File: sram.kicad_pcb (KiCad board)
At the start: 4 copper layers, 92 x 47 mm, 28 parts, among them J1 Cache_slot, U1 IS61C256AL-12JLI, U10 74F244, U11 74F244, U2 IS61C256AL-12JLI, U3 IS61C256AL-12JLI, U4 IS61C256AL-12JLI, U5 IS61C256AL-12JLI, U6 IS61C256AL-12JLI, U7 IS61C256AL-12JLI, U8 IS61C256AL-12JLI, U9 IS61C3216AL-12TLI

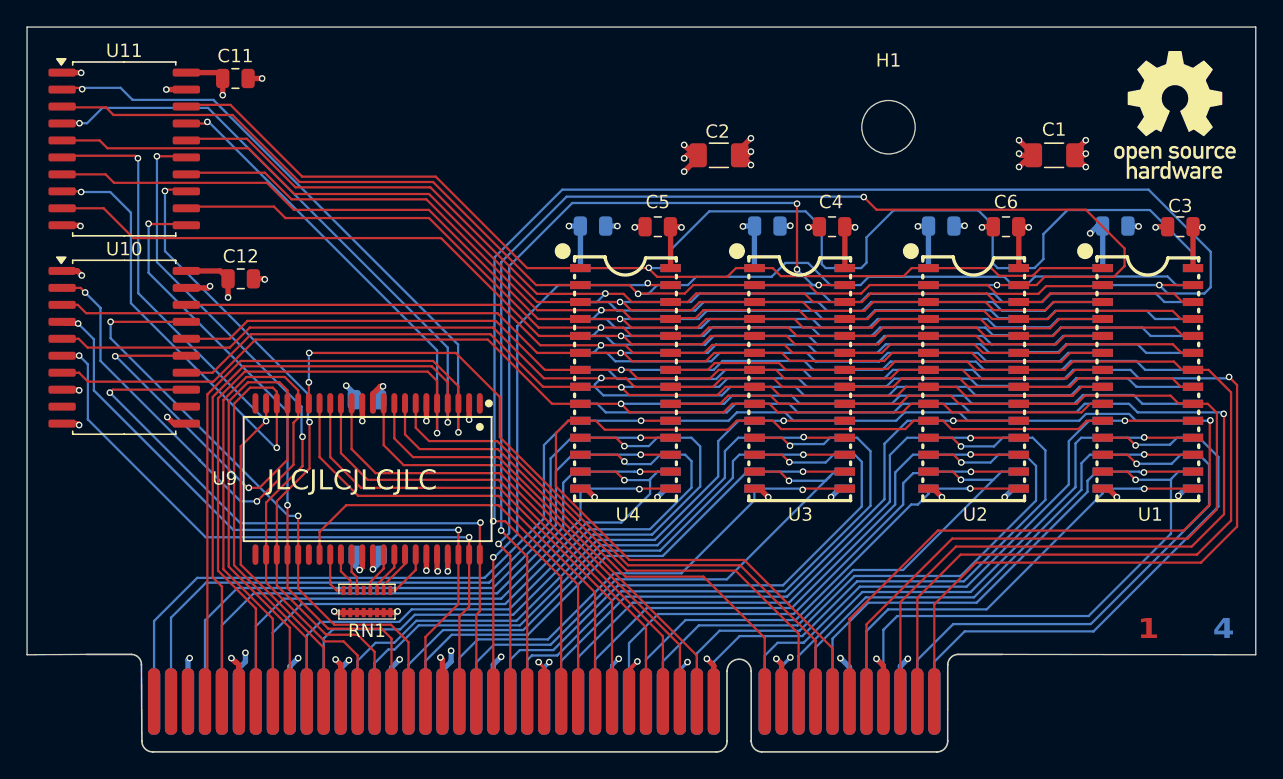
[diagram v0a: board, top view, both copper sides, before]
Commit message: change from rasz_pl:  - moving VIAs apart  - change resistor network with single resistor
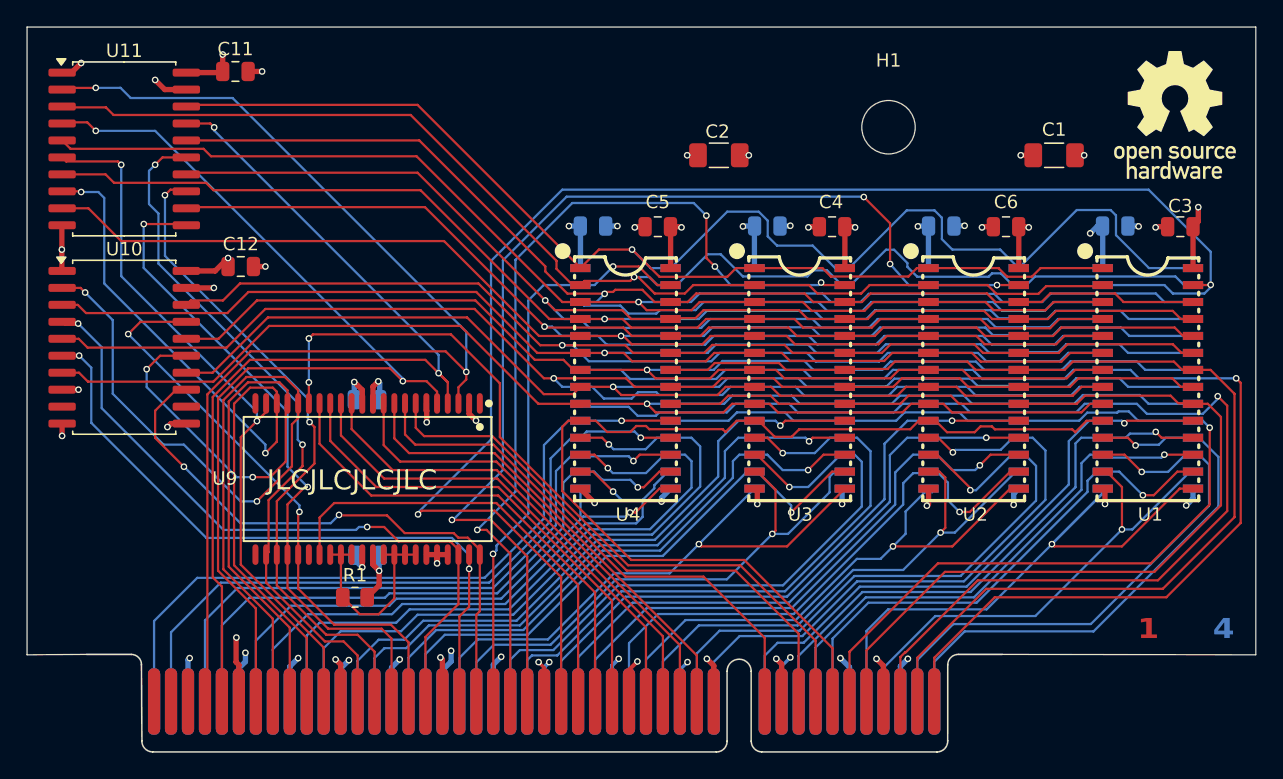
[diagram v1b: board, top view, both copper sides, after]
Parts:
- removed RN1: EXB2HV103JV, footprints:RES-ARRAY-SMD_16P-L3.8-W1.6-P0.50-BL
- added R1: 10k, Resistor_SMD:R_0805_2012Metric, F.Cu at (163.6, 99.7)
- moved C12 0.92 mm to (155.0, 74.9)
- moved C11 0.52 mm to (154.6, 60.3)
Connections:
- U11 pad 17: CPU_A15 -> CPU_A16
- U11 pad 4: CPU_A16 -> CPU_A15
- U9 pad 30: TIO9 -> TIO10
- U9 pad 32: TIO11 -> TIO10
- U9 pad 35: TIO12 -> TIO10
- U9 pad 36: TIO13 -> TIO10
- U9 pad 37: TIO14 -> TIO10
- U9 pad 38: TIO15 -> TIO10
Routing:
- net CWE1: track 100.6 -> 83.9 mm, vias 3 -> 4
- net CPU_A16: track 87.6 -> 72.7 mm
- net TIO10: track 2.97 -> 15.4 mm
- net CPU_D3: track 34.4 -> 45.4 mm
- net GND: track 99.6 -> 92.2 mm, vias 54 -> 44
- net CWE0: track 107.3 -> 114.0 mm
- net CPU_A4: track 51.2 -> 44.8 mm
- net CPU_D11: track 36.6 -> 42.8 mm
- net CPU_D19: track 38.0 -> 43.4 mm
- net +5V: track 81.3 -> 76.6 mm, vias 27 -> 23
- net CPU_A13: track 58.0 -> 53.4 mm
- net CPU_D2: track 41.2 -> 36.9 mm
- net Cache_A15: track 129.3 -> 133.4 mm
- net CWE2: track 70.6 -> 66.7 mm
- net TIO15: track 3.68 -> 0.00 mm
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
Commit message: pass DRC with rounded tracks
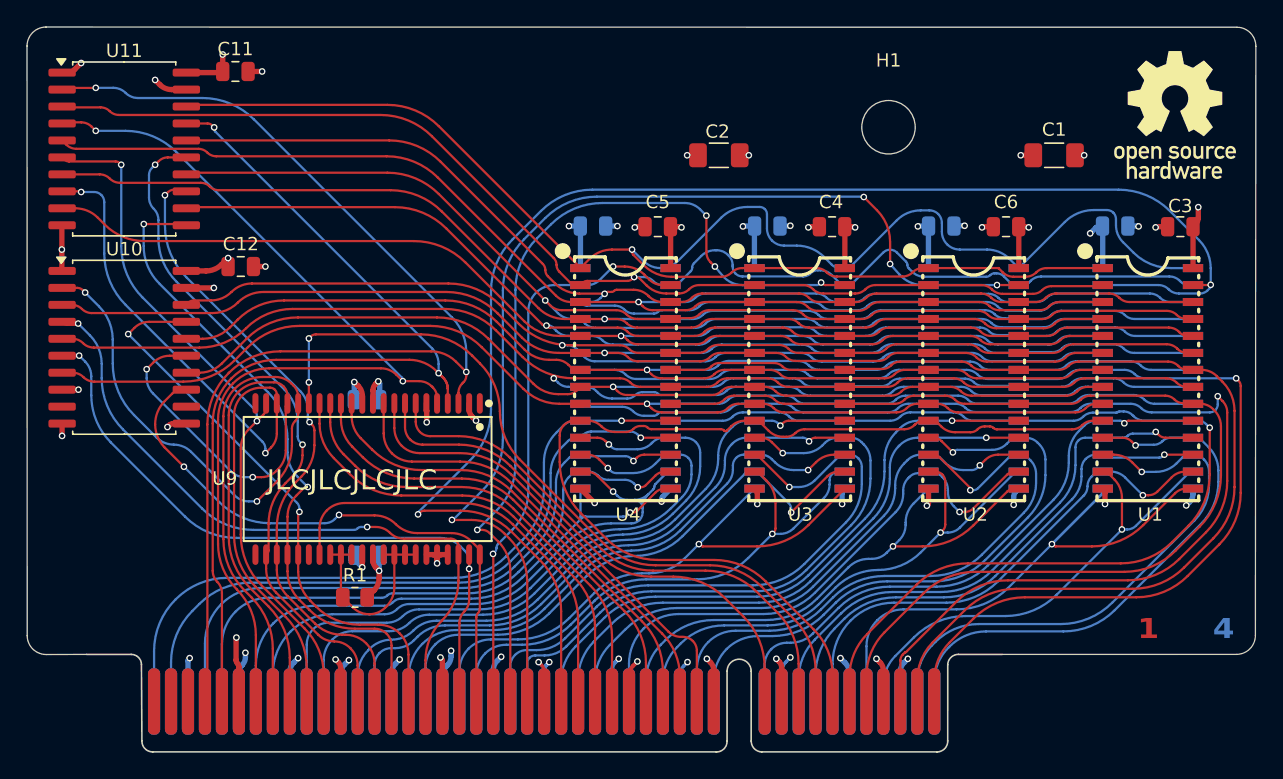
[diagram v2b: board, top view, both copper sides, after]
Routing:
- net Cache_A13: track 133.5 -> 130.8 mm
- net Cache_A4: track 126.4 -> 124.1 mm
- net Cache_A16: track 125.4 -> 123.3 mm
- net Cache_A14: track 122.0 -> 120.0 mm
- net CWE0: track 114.0 -> 111.9 mm
- net Cache_A5: track 119.5 -> 117.5 mm
- net Cache_A7: track 127.9 -> 125.9 mm
- net Cache_A6: track 116.0 -> 113.9 mm
- net CA3A: track 77.8 -> 75.8 mm
- net Cache_A8: track 127.8 -> 125.9 mm
- net CPU_A14: track 64.9 -> 63.0 mm
- net Cache_A12: track 124.7 -> 122.8 mm
- net Cache_A17: track 132.3 -> 130.4 mm
- net COEA: track 85.0 -> 83.3 mm
- net COEB: track 92.4 -> 90.6 mm
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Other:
- outline, holes or cut-outs redrawn

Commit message: updated to 256KB/1MB
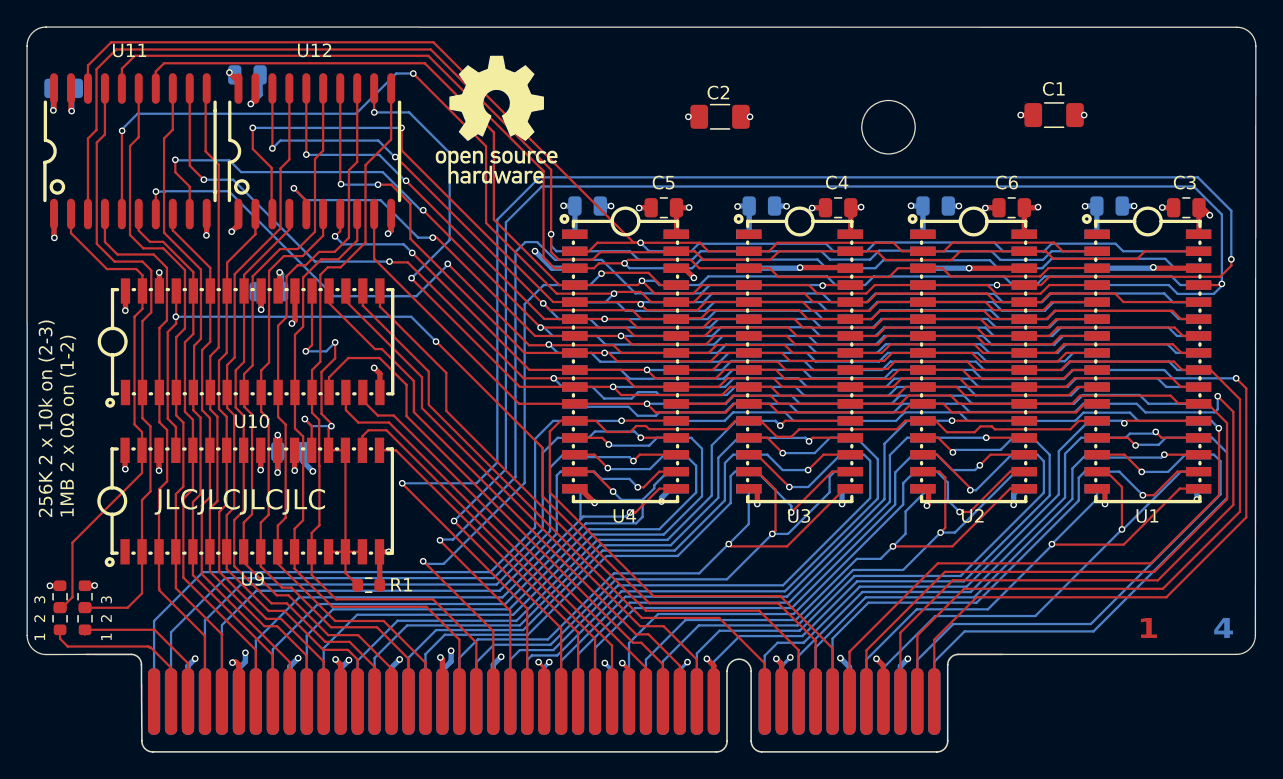
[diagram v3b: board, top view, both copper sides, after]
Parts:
- added R2: 0, Resistor_SMD:R_0603_1608Metric, F.Cu at (143.3, 101.3)
- added R3: 0, Resistor_SMD:R_0603_1608Metric, F.Cu at (141.5, 101.3)
- added R4: 10k, Resistor_SMD:R_0603_1608Metric, F.Cu at (143.3, 99.7)
- added R5: 10k, Resistor_SMD:R_0603_1608Metric, F.Cu at (141.5, 99.7)
- added U12: SN74AHCT244DWR, others:SOIC-20_L12.8-W7.5-P1.27-LS10.3-BL, F.Cu at (160.5, 66.3)
- C11, C12: moved to B.Cu
- J1: footprint footprints:Cache slot -> others:Cache slot
- R1: footprint Resistor_SMD:R_0805_2012Metric -> Resistor_SMD:R_0603_1608Metric
- U1, U2, U3, U4, U5, U6, U7, U8: value IS61C256AL-12JLI -> IS61C1024AL-12JLI; footprint footprints:SOJ-28_L18.1-W7.6-P1.27-LS8.6-BL -> others:SOJ-32_L21.0-W7.6-P1.27-LS8.5-BL
- U10: value 74F244 -> IS61C1024AL-12JLI; footprint Package_SO:SOIC-20W_7.5x12.8mm_P1.27mm -> others:SOJ-32_L21.0-W7.6-P1.27-LS8.5-BL
- U11: value 74F244 -> SN74AHCT244DWR; footprint Package_SO:SOIC-20W_7.5x12.8mm_P1.27mm -> others:SOIC-20_L12.8-W7.5-P1.27-LS10.3-BL
- U9: value IS61C3216AL-12TLI -> IS61C1024AL-12JLI; footprint footprints:TSOP-44_L18.4-W10.2-P0.80-LS11.8-BL -> others:SOJ-32_L21.0-W7.6-P1.27-LS8.5-BL
- moved C12 18.8 mm to (141.7, 61.6)
- moved C13 10.9 mm to (157.1, 76.8)
- moved C14 9.68 mm to (158.7, 88.8)
- moved U10 9.62 mm to (155.9, 80.6)
- moved U9 8.80 mm to (155.9, 92.5), turned to 0 degrees
- moved C1 3.01 mm to (215.9, 63.6)
- moved C2 2.88 mm to (190.9, 63.7)
- moved C7 1.56 mm to (220.1, 70.4)
- moved C8 1.56 mm to (207.0, 70.4)
- moved C10 1.55 mm to (194.0, 70.4)
- moved C9 1.55 mm to (181.0, 70.4)
- moved C5 1.49 mm to (186.7, 70.5)
- moved C4 1.49 mm to (199.7, 70.5)
- moved C3 1.49 mm to (225.8, 70.5)
- moved C6 1.48 mm to (212.7, 70.5)
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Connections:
- J1 pad a45: unconnected-(J1-Pada45) -> CPU_A18
- J1 pad a46: unconnected-(J1-Pada46) -> CPU_A19
- U1 pad 1: Cache_A17 -> unconnected-(U1-NC-Pad1)
- U1 pad 10: CA3A -> Cache_A5
- U1 pad 11: CPU_D0 -> Cache_A4
- U1 pad 12: CPU_D1 -> CA3A
- U1 pad 13: CPU_D2 -> CPU_D0
- U1 pad 14: GND -> CPU_D1
- U1 pad 15: CPU_D3 -> CPU_D2
- U1 pad 16: CPU_D4 -> GND
- U1 pad 17: CPU_D5 -> CPU_D3
- U1 pad 18: CPU_D6 -> CPU_D4
- U1 pad 19: CPU_D7 -> CPU_D5
- U1 pad 2: Cache_A15 -> Cache_A19
- U1 pad 20: CCSA -> CPU_D6
- U1 pad 21: Cache_A13 -> CPU_D7
- U1 pad 22: COEA -> CCSA
- U1 pad 23: Cache_A14 -> Cache_A13
- U1 pad 24: Cache_A12 -> COEA
- U1 pad 25: Cache_A11 -> Cache_A14
- U1 pad 26: Cache_A16 -> Cache_A12
- U1 pad 27: CWE0 -> Cache_A11
- U1 pad 28: +5V -> Cache_A16
- U1 pad 3: Cache_A10 -> Cache_A17
- U1 pad 4: Cache_A9 -> Cache_A15
- U1 pad 5: Cache_A8 -> Cache_A10
- U1 pad 6: Cache_A7 -> Cache_A9
- U1 pad 7: Cache_A6 -> Cache_A8
- U1 pad 8: Cache_A5 -> Cache_A7
- U1 pad 9: Cache_A4 -> Cache_A6
- U10 pad 1: GND -> unconnected-(U10-NC-Pad1)
- U10 pad 10: GND -> CPU_A6
- U10 pad 11: GND -> CPU_A5
- U10 pad 12: unconnected-(U10-1Y3-Pad12) -> CPU_A4
- U10 pad 13: CPU_A4 -> TAG_Q4
- U10 pad 14: Cache_A5 -> TAG_Q6
- U10 pad 15: CPU_A13 -> TAG_Q5
- U10 pad 16: Cache_A6 -> GND
- U10 pad 17: CPU_A7 -> TAG_Q0
- U10 pad 18: Cache_A14 -> TAG_Q1
- U10 pad 19: GND -> TAG_Q2
- U10 pad 2: CPU_A14 -> JPU_A18
- U10 pad 20: +5V -> TAG_Q3
- U10 pad 3: Cache_A7 -> CPU_A17
- U10 pad 4: CPU_A6 -> CPU_A16
- U10 pad 5: Cache_A13 -> CPU_A14
- U10 pad 6: CPU_A5 -> CPU_A12
- U10 pad 7: Cache_A4 -> CPU_A10
- U10 pad 8: GND -> CPU_A8
- U10 pad 9: unconnected-(U10-2Y3-Pad9) -> CPU_A7
- U11 pad 11: CPU_A8 -> CPU_A12
- U11 pad 12: Cache_A12 -> Cache_A13
- U11 pad 13: CPU_A9 -> CPU_A14
- U11 pad 14: Cache_A11 -> Cache_A15
- U11 pad 15: CPU_A10 -> CPU_A16
- U11 pad 16: Cache_A16 -> Cache_A17
- U11 pad 17: CPU_A16 -> JPU_A18
- U11 pad 18: Cache_A17 -> Cache_A19
- U11 pad 2: CPU_A17 -> JPU_A19
- U11 pad 3: Cache_A15 -> Cache_A18
- U11 pad 4: CPU_A15 -> CPU_A17
- U11 pad 5: Cache_A10 -> Cache_A16
- U11 pad 6: CPU_A11 -> CPU_A15
- U11 pad 7: Cache_A9 -> Cache_A14
- U11 pad 8: CPU_A12 -> CPU_A13
- U11 pad 9: Cache_A8 -> Cache_A12
- U2 pad 1: Cache_A17 -> unconnected-(U2-NC-Pad1)
- U2 pad 10: CA3A -> Cache_A5
- U2 pad 11: CPU_D8 -> Cache_A4
- U2 pad 12: CPU_D9 -> CA3A
- U2 pad 13: CPU_D10 -> CPU_D8
- U2 pad 14: GND -> CPU_D9
- U2 pad 15: CPU_D11 -> CPU_D10
- U2 pad 16: CPU_D12 -> GND
- U2 pad 17: CPU_D13 -> CPU_D11
- U2 pad 18: CPU_D14 -> CPU_D12
- U2 pad 19: CPU_D15 -> CPU_D13
- U2 pad 2: Cache_A15 -> Cache_A19
- U2 pad 20: CCSA -> CPU_D14
- U2 pad 21: Cache_A13 -> CPU_D15
- U2 pad 22: COEA -> CCSA
- U2 pad 23: Cache_A14 -> Cache_A13
- U2 pad 24: Cache_A12 -> COEA
- U2 pad 25: Cache_A11 -> Cache_A14
- U2 pad 26: Cache_A16 -> Cache_A12
- U2 pad 27: CWE1 -> Cache_A11
- U2 pad 28: +5V -> Cache_A16
- U2 pad 3: Cache_A10 -> Cache_A17
- U2 pad 4: Cache_A9 -> Cache_A15
- U2 pad 5: Cache_A8 -> Cache_A10
- U2 pad 6: Cache_A7 -> Cache_A9
- U2 pad 7: Cache_A6 -> Cache_A8
- U2 pad 8: Cache_A5 -> Cache_A7
- U2 pad 9: Cache_A4 -> Cache_A6
- U3 pad 1: Cache_A17 -> unconnected-(U3-NC-Pad1)
- U3 pad 10: CA3A -> Cache_A5
- U3 pad 11: CPU_D16 -> Cache_A4
- U3 pad 12: CPU_D17 -> CA3A
- U3 pad 13: CPU_D18 -> CPU_D16
- U3 pad 14: GND -> CPU_D17
- U3 pad 15: CPU_D19 -> CPU_D18
- U3 pad 16: CPU_D20 -> GND
- U3 pad 17: CPU_D21 -> CPU_D19
- U3 pad 18: CPU_D22 -> CPU_D20
- U3 pad 19: CPU_D23 -> CPU_D21
- U3 pad 2: Cache_A15 -> Cache_A19
- U3 pad 20: CCSA -> CPU_D22
- U3 pad 21: Cache_A13 -> CPU_D23
- U3 pad 22: COEA -> CCSA
- U3 pad 23: Cache_A14 -> Cache_A13
- U3 pad 24: Cache_A12 -> COEA
- U3 pad 25: Cache_A11 -> Cache_A14
- U3 pad 26: Cache_A16 -> Cache_A12
- U3 pad 27: CWE2 -> Cache_A11
- U3 pad 28: +5V -> Cache_A16
- U3 pad 3: Cache_A10 -> Cache_A17
- U3 pad 4: Cache_A9 -> Cache_A15
- U3 pad 5: Cache_A8 -> Cache_A10
- U3 pad 6: Cache_A7 -> Cache_A9
- U3 pad 7: Cache_A6 -> Cache_A8
- U3 pad 8: Cache_A5 -> Cache_A7
- U3 pad 9: Cache_A4 -> Cache_A6
- U4 pad 1: Cache_A17 -> unconnected-(U4-NC-Pad1)
- U4 pad 10: CA3A -> Cache_A5
- U4 pad 11: CPU_D24 -> Cache_A4
- U4 pad 12: CPU_D25 -> CA3A
- U4 pad 13: CPU_D26 -> CPU_D24
- U4 pad 14: GND -> CPU_D25
- U4 pad 15: CPU_D27 -> CPU_D26
- U4 pad 16: CPU_D28 -> GND
- U4 pad 17: CPU_D29 -> CPU_D27
- U4 pad 18: CPU_D30 -> CPU_D28
- U4 pad 19: CPU_D31 -> CPU_D29
- U4 pad 2: Cache_A15 -> Cache_A19
- U4 pad 20: CCSA -> CPU_D30
- U4 pad 21: Cache_A13 -> CPU_D31
- U4 pad 22: COEA -> CCSA
- U4 pad 23: Cache_A14 -> Cache_A13
- U4 pad 24: Cache_A12 -> COEA
- U4 pad 25: Cache_A11 -> Cache_A14
- U4 pad 26: Cache_A16 -> Cache_A12
- U4 pad 27: CWE3 -> Cache_A11
- U4 pad 28: +5V -> Cache_A16
- U4 pad 3: Cache_A10 -> Cache_A17
- U4 pad 4: Cache_A9 -> Cache_A15
- U4 pad 5: Cache_A8 -> Cache_A10
- U4 pad 6: Cache_A7 -> Cache_A9
- U4 pad 7: Cache_A6 -> Cache_A8
- U4 pad 8: Cache_A5 -> Cache_A7
- U4 pad 9: Cache_A4 -> Cache_A6
- U5 pad 1: Cache_A17 -> unconnected-(U5-NC-Pad1)
- U5 pad 10: CA3BA2 -> Cache_A5
- U5 pad 11: CPU_D0 -> Cache_A4
- U5 pad 12: CPU_D1 -> CA3BA2
- U5 pad 13: CPU_D2 -> CPU_D0
- U5 pad 14: GND -> CPU_D1
- U5 pad 15: CPU_D3 -> CPU_D2
- U5 pad 16: CPU_D4 -> GND
- U5 pad 17: CPU_D5 -> CPU_D3
- U5 pad 18: CPU_D6 -> CPU_D4
- U5 pad 19: CPU_D7 -> CPU_D5
- U5 pad 2: Cache_A15 -> Cache_A19
- U5 pad 20: CCSB -> CPU_D6
- U5 pad 21: Cache_A13 -> CPU_D7
- U5 pad 22: COEB -> CCSB
- U5 pad 23: Cache_A14 -> Cache_A13
- U5 pad 24: Cache_A12 -> COEB
- U5 pad 25: Cache_A11 -> Cache_A14
- U5 pad 26: Cache_A16 -> Cache_A12
- U5 pad 27: CWE0 -> Cache_A11
- U5 pad 28: +5V -> Cache_A16
- U5 pad 3: Cache_A10 -> Cache_A17
- U5 pad 4: Cache_A9 -> Cache_A15
- U5 pad 5: Cache_A8 -> Cache_A10
- U5 pad 6: Cache_A7 -> Cache_A9
- U5 pad 7: Cache_A6 -> Cache_A8
- U5 pad 8: Cache_A5 -> Cache_A7
- U5 pad 9: Cache_A4 -> Cache_A6
- U6 pad 1: Cache_A17 -> unconnected-(U6-NC-Pad1)
- U6 pad 10: CA3BA2 -> Cache_A5
- U6 pad 11: CPU_D8 -> Cache_A4
- U6 pad 12: CPU_D9 -> CA3BA2
- U6 pad 13: CPU_D10 -> CPU_D8
- U6 pad 14: GND -> CPU_D9
- U6 pad 15: CPU_D11 -> CPU_D10
- U6 pad 16: CPU_D12 -> GND
- U6 pad 17: CPU_D13 -> CPU_D11
- U6 pad 18: CPU_D14 -> CPU_D12
- U6 pad 19: CPU_D15 -> CPU_D13
- U6 pad 2: Cache_A15 -> Cache_A19
- U6 pad 20: CCSB -> CPU_D14
- U6 pad 21: Cache_A13 -> CPU_D15
- U6 pad 22: COEB -> CCSB
- U6 pad 23: Cache_A14 -> Cache_A13
- U6 pad 24: Cache_A12 -> COEB
- U6 pad 25: Cache_A11 -> Cache_A14
- U6 pad 26: Cache_A16 -> Cache_A12
- U6 pad 27: CWE1 -> Cache_A11
- U6 pad 28: +5V -> Cache_A16
- U6 pad 3: Cache_A10 -> Cache_A17
- U6 pad 4: Cache_A9 -> Cache_A15
- U6 pad 5: Cache_A8 -> Cache_A10
- U6 pad 6: Cache_A7 -> Cache_A9
- U6 pad 7: Cache_A6 -> Cache_A8
- U6 pad 8: Cache_A5 -> Cache_A7
- U6 pad 9: Cache_A4 -> Cache_A6
- U7 pad 1: Cache_A17 -> unconnected-(U7-NC-Pad1)
- U7 pad 10: CA3BA2 -> Cache_A5
- U7 pad 11: CPU_D16 -> Cache_A4
- U7 pad 12: CPU_D17 -> CA3BA2
- U7 pad 13: CPU_D18 -> CPU_D16
- U7 pad 14: GND -> CPU_D17
- U7 pad 15: CPU_D19 -> CPU_D18
- U7 pad 16: CPU_D20 -> GND
- U7 pad 17: CPU_D21 -> CPU_D19
- U7 pad 18: CPU_D22 -> CPU_D20
- U7 pad 19: CPU_D23 -> CPU_D21
- U7 pad 2: Cache_A15 -> Cache_A19
- U7 pad 20: CCSB -> CPU_D22
- U7 pad 21: Cache_A13 -> CPU_D23
- U7 pad 22: COEB -> CCSB
- U7 pad 23: Cache_A14 -> Cache_A13
- U7 pad 24: Cache_A12 -> COEB
- U7 pad 25: Cache_A11 -> Cache_A14
- U7 pad 26: Cache_A16 -> Cache_A12
- U7 pad 27: CWE2 -> Cache_A11
- U7 pad 28: +5V -> Cache_A16
- U7 pad 3: Cache_A10 -> Cache_A17
- U7 pad 4: Cache_A9 -> Cache_A15
- U7 pad 5: Cache_A8 -> Cache_A10
- U7 pad 6: Cache_A7 -> Cache_A9
- U7 pad 7: Cache_A6 -> Cache_A8
- U7 pad 8: Cache_A5 -> Cache_A7
- U7 pad 9: Cache_A4 -> Cache_A6
- U8 pad 1: Cache_A17 -> unconnected-(U8-NC-Pad1)
- U8 pad 10: CA3BA2 -> Cache_A5
- U8 pad 11: CPU_D24 -> Cache_A4
- U8 pad 12: CPU_D25 -> CA3BA2
- U8 pad 13: CPU_D26 -> CPU_D24
- U8 pad 14: GND -> CPU_D25
- U8 pad 15: CPU_D27 -> CPU_D26
- U8 pad 16: CPU_D28 -> GND
- U8 pad 17: CPU_D29 -> CPU_D27
- U8 pad 18: CPU_D30 -> CPU_D28
- U8 pad 19: CPU_D31 -> CPU_D29
- U8 pad 2: Cache_A15 -> Cache_A19
- U8 pad 20: CCSB -> CPU_D30
- U8 pad 21: Cache_A13 -> CPU_D31
- U8 pad 22: COEB -> CCSB
- U8 pad 23: Cache_A14 -> Cache_A13
- U8 pad 24: Cache_A12 -> COEB
- U8 pad 25: Cache_A11 -> Cache_A14
- U8 pad 26: Cache_A16 -> Cache_A12
- U8 pad 27: CWE3 -> Cache_A11
- U8 pad 28: +5V -> Cache_A16
- U8 pad 3: Cache_A10 -> Cache_A17
- U8 pad 4: Cache_A9 -> Cache_A15
- U8 pad 5: Cache_A8 -> Cache_A10
- U8 pad 6: Cache_A7 -> Cache_A9
- U8 pad 7: Cache_A6 -> Cache_A8
- U8 pad 8: Cache_A5 -> Cache_A7
- U8 pad 9: Cache_A4 -> Cache_A6
- U9 pad 10: TAG_Q3 -> CPU_A6
- U9 pad 11: +5V -> CPU_A5
- U9 pad 12: GND -> CPU_A4
- U9 pad 13: TAG_Q4 -> TIO10
- U9 pad 14: TAG_Q5 -> TIO10
- U9 pad 15: TAG_Q6 -> TIO10
- U9 pad 16: TAG_Q7 -> GND
- U9 pad 17: TAG_WE -> TAG_Q8
- U9 pad 18: CPU_A14 -> TAG_Q7
- U9 pad 19: CPU_A13 -> TIO10
- U9 pad 2: +5V -> JPU_A18
- U9 pad 20: CPU_A12 -> TIO10
- U9 pad 21: CPU_A11 -> TIO10
- U9 pad 22: unconnected-(U9-NC-Pad22) -> GND
- U9 pad 23: unconnected-(U9-NC-Pad23) -> +5V
- U9 pad 24: CPU_A10 -> GND
- U9 pad 26: CPU_A8 -> CPU_A11
- U9 pad 27: CPU_A7 -> CPU_A13
- U9 pad 28: unconnected-(U9-NC-Pad28) -> CPU_A15
- U9 pad 29: TAG_Q8 -> TAG_WE
- U9 pad 30: TIO10 -> +5V
- U9 pad 31: TIO10 -> JPU_A19
- U9 pad 32: TIO10 -> +5V
- U9 pad 5: CPU_A15 -> CPU_A14
- U9 pad 6: GND -> CPU_A12
- U9 pad 7: TAG_Q0 -> CPU_A10
- U9 pad 8: TAG_Q1 -> CPU_A8
- U9 pad 9: TAG_Q2 -> CPU_A7
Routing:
- net Cache_A18: track 0.00 -> 149.8 mm, vias 0 -> 1
- net Cache_A19: track 0.00 -> 135.1 mm, vias 0 -> 1
- net CWE1: track 82.4 -> 130.9 mm, vias 4 -> 3
- net JPU_A18: track 0.00 -> 46.6 mm
- net CPU_A17: track 86.6 -> 42.2 mm, vias 2 -> 0
- net JPU_A19: track 0.00 -> 36.1 mm
- net CPU_A15: track 75.1 -> 41.8 mm, vias 2 -> 0
- net +5V: track 76.0 -> 98.9 mm, vias 23 -> 32
- net Cache_A16: track 123.3 -> 145.2 mm, vias 1 -> 3
- net CPU_A16: track 72.2 -> 50.9 mm, vias 2 -> 0
- net TIO10: track 15.1 -> 35.2 mm, vias 0 -> 4
- net TAG_WE: track 57.9 -> 77.1 mm
- net Cache_A4: track 124.1 -> 106.4 mm
- net CPU_A4: track 43.8 -> 58.7 mm, vias 2 -> 0
- net CPU_A14: track 63.0 -> 50.5 mm, vias 2 -> 0
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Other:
- board text added: "1 2 3"
- board text added: "256K 2 x 10k on (2-3) 1MB 2 x 0Ω on (1-2)"
- board text added: "MODEL: COMPAQ CACHE MODULE TYPE: 197005-001"
- board text removed: "MODEL: COMPAQ 256KB CACHE MODULE TYPE: 197005-001"

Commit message: cleanup
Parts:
- moved C11 1.01 mm to (155.5, 61.6)
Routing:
- net +5V: track 98.9 -> 99.8 mm
- net CPU_A6: track 56.6 -> 57.4 mm
- net CPU_A9: track 47.4 -> 48.3 mm
- net CPU_A8: track 58.6 -> 59.4 mm
- net CA3BA2: track 83.7 -> 84.4 mm
- net CPU_D13: track 44.1 -> 44.8 mm
- net CPU_A10: track 54.1 -> 54.8 mm
- net CPU_D14: track 45.3 -> 46.0 mm
- net CPU_A7: track 46.7 -> 47.4 mm
- net CPU_D15: track 47.2 -> 47.8 mm
- net TAG_Q0: track 48.7 -> 49.3 mm
- net CPU_D21: track 44.8 -> 45.4 mm
- net CPU_D20: track 45.3 -> 45.9 mm

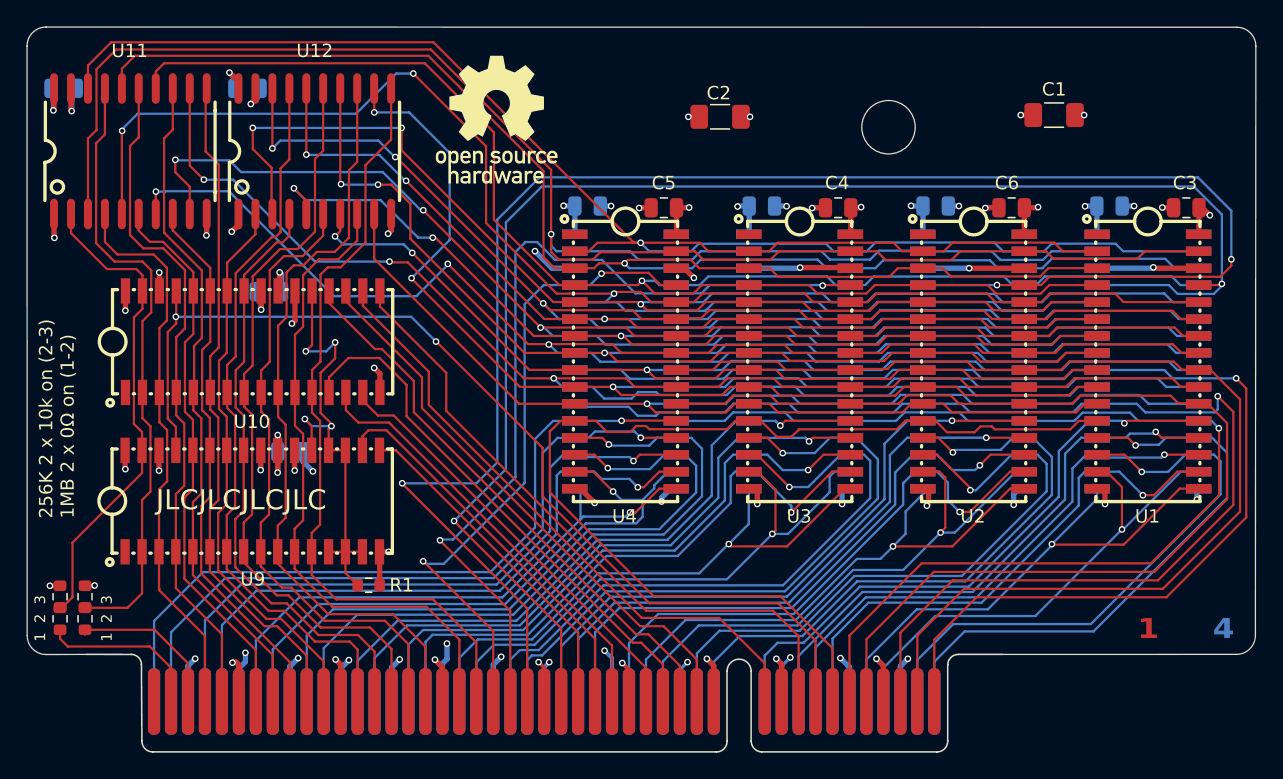
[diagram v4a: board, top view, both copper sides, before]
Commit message: added switch to set memory size
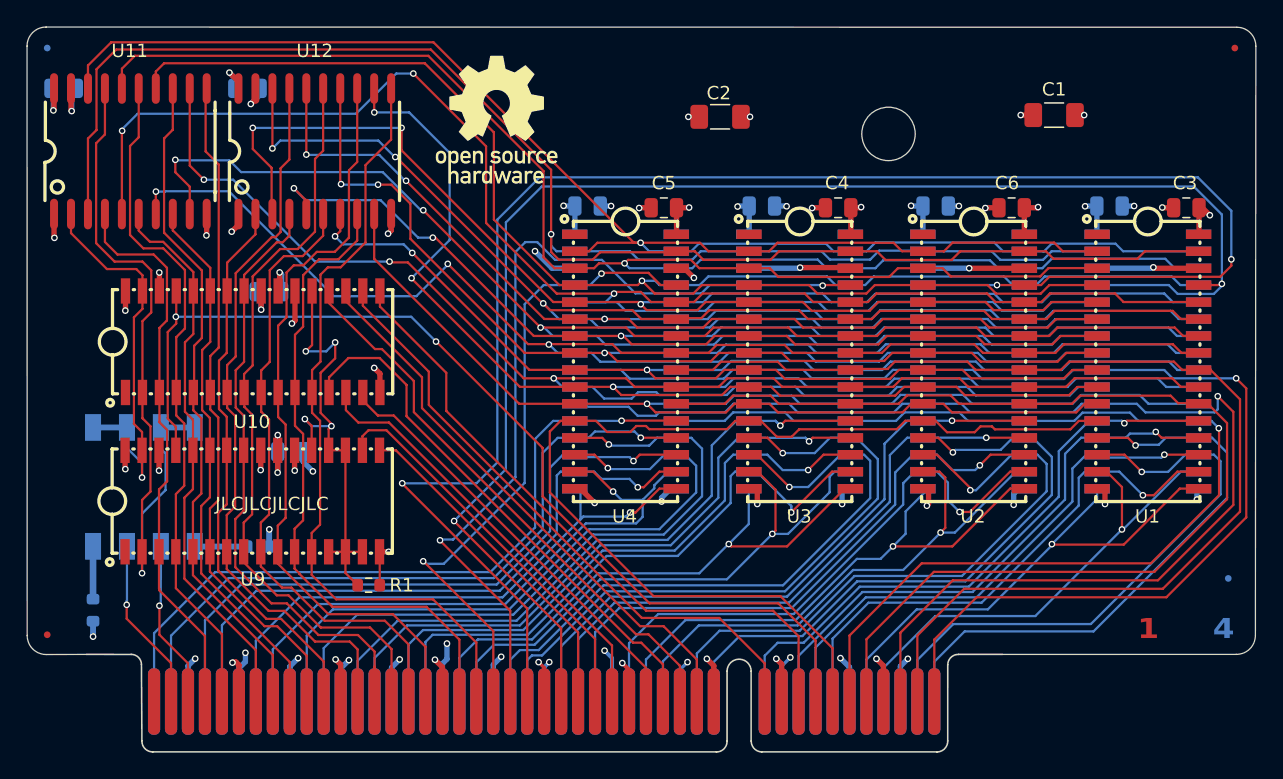
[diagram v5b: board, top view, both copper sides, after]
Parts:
- removed R4, R5: 10k, Resistor_SMD:R_0603_1608Metric
- added FID1: Fiducial, Fiducial:Fiducial_0.5mm_Mask1mm, F.Cu at (140.5, 102.5)
- added FID2: Fiducial, Fiducial:Fiducial_0.5mm_Mask1mm, F.Cu at (229.4, 58.6)
- added FID3: Fiducial, Fiducial:Fiducial_0.5mm_Mask1mm, B.Cu at (140.5, 58.6)
- added FID4: Fiducial, Fiducial:Fiducial_0.5mm_Mask1mm, B.Cu at (228.9, 98.3)
- added SW1: DSIC04TSGET, others:SW-SMD_8P-L11.1-W6.2-P2.54-LS9.8, B.Cu at (147.8, 91.4)
- R2, R3: value 0 -> 10k; moved to B.Cu
- moved R3 15.8 mm to (156.3, 95.9), turned to 180 degrees
- moved R2 0.88 mm to (143.9, 100.7)
- moved H1 0.50 mm to (203.5, 65.0)
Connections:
- R2 pad 1: CPU_A18 -> GND
- R2 pad 2: JPU_A18 -> Net-(SW1-A4)
- R3 pad 1: CPU_A19 -> GND
- R3 pad 2: JPU_A19 -> Net-(SW1-A1)
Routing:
- net JPU_A18: track 46.7 -> 54.8 mm, vias 0 -> 1
- net JPU_A19: track 36.1 -> 30.5 mm, vias 0 -> 1
- net Net-(SW1-A4): track 0.00 -> 3.95 mm
- net Net-(SW1-A1): track 0.00 -> 3.92 mm
- net GND: track 96.1 -> 97.1 mm
- net CPU_A19: track 12.4 -> 13.0 mm, vias 0 -> 1
- net CPU_A18: track 12.0 -> 12.6 mm, vias 0 -> 1
- net CPU_D31: track 54.8 -> 54.3 mm
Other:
- board text added: "1MB 2,3 1,4 512K 2,4 1,3 256K 1,4 2,3"
- board text added: "OFF"
- board text added: "ON"
- board text removed: "1 2 3"
- board text removed: "256K 2 x 10k on (2-3) 1MB 2 x 0Ω on (1-2)"
